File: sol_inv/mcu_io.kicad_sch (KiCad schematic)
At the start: 33 parts, among them J11 Conn_01x05, J3 Conn_01x06, J4 Conn_01x05, J5 Conn_ARM_JTAG_SWD_10, J6 Conn_01x05, J7 Conn_01x02, J8 Conn_01x08, J9 Conn_01x08, SW2 SW_Push_Dual, SW3 SW_Push_Dual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

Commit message: v0.2 components change + reference to providers
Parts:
- C21: renamed from C19; footprint Capacitor_SMD:C_1206_3216Metric -> Capacitor_SMD:C_0201_0603Metric; ComponentLink2URL (none) -> https://ro.farnell.com/wurth-elektronik/885012104002/cap-0-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
- C22: renamed from C20; footprint Capacitor_SMD:C_1206_3216Metric -> Capacitor_SMD:C_0201_0603Metric; ComponentLink2URL (none) -> https://ro.farnell.com/wurth-elektronik/885012104002/cap-0-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
- C23: renamed from C21; footprint Capacitor_SMD:C_1206_3216Metric -> Capacitor_SMD:C_0201_0603Metric; ComponentLink2URL (none) -> https://ro.farnell.com/wurth-elektronik/885012104002/cap-0-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
- C24: renamed from C22; value 18-23nF -> 22pF; ComponentLink2URL (none) -> https://ro.farnell.com/vishay/vj0805a220gxqcw1bc/cap-22pf-1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; now not fitted; now left out of the parts list
- C25: renamed from C23; value 7-11nF -> 8pF; ComponentLink2URL (none) -> https://ro.farnell.com/tdk/cga2b2np01h080d050ba/cap-8pf-50v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; now not fitted; now left out of the parts list
- C26: renamed from C24; value 18-23nF -> 22pF; ComponentLink2URL (none) -> https://ro.farnell.com/vishay/vj0805a220gxqcw1bc/cap-22pf-1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; now not fitted; now left out of the parts list
- C27: renamed from C25; value 7-11nF -> 8pF; ComponentLink2URL (none) -> https://ro.farnell.com/tdk/cga2b2np01h080d050ba/cap-8pf-50v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; now not fitted; now left out of the parts list
- D1, D2, D3: ComponentLink2URL (none) -> https://ro.farnell.com/kingbright/kp-2012syck/led-alingap-s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
- J10: renamed from J6; ComponentLink2URL (none) -> https://ro.farnell.com/multicomp-pro/2212s-05sg-85/socket-p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
- J3: footprint Connector_PinSocket_2.54mm:PinSocket_1x06_P2.54mm_Vertical -> Connector_PinHeader_2.54mm:PinHeader_1x06_P2.54mm_Vertical; ComponentLink2URL (none) -> https://ro.farnell.com/samtec/tsw-106-07-l-s/header-2-54mm-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
- J4: ComponentLink2URL (none) -> https://ro.farnell.com/multicomp-pro/2212s-05sg-85/socket-p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
- J5: ComponentLink2URL (none) -> https://ro.farnell.com/wurth-elektronik/62701021621/conn-he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
- J6: renamed from J7; ComponentLink2URL (none) -> https://ro.farnell.com/multicomp-pro/2212s-02sg-85/conn-rcp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
- J7: renamed from J8; ComponentLink2URL (none) -> https://ro.farnell.com/multicomp-pro/2212s-08sg-85/conn-rcp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
- J8: renamed from J9; ComponentLink2URL (none) -> https://ro.farnell.com/multicomp-pro/2212s-08sg-85/conn-rcp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
- J9: renamed from J11; ComponentLink2URL (none) -> https://ro.farnell.com/multicomp-pro/2212s-05sg-85/socket-p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
- R18, R19: ComponentLink2URL (none) -> https://ro.farnell.com/multicomp-pro/mcmr08x1001ftl/res-1k-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
- R20: renamed from R21; ComponentLink2URL (none) -> https://ro.farnell.com/multicomp-pro/mcmr08x1001ftl/res-1k-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
- R21: renamed from R20; ComponentLink2URL (none) -> https://ro.farnell.com/multicomp-pro/mcmr08x1001ftl/res-1k-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
- R22: ComponentLink2URL (none) -> https://ro.farnell.com/multicomp-pro/mcmr12x20r0ftl/res-20r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
- R23, R24, R25: value 82R -> 330R; footprint Resistor_SMD:R_0402_1005Metric -> Resistor_SMD:R_0603_1608Metric; ComponentLink2URL (none) -> https://ro.farnell.com/te-connectivity/crgcq0603j330r/res-3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
- R26, R27: ComponentLink2URL (none) -> https://ro.farnell.com/multicomp-pro/mcmr04x4701ftl/res-4k7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
- SW2, SW3: ComponentLink2URL (none) -> https://ro.mouser.com/ProductDetail/Omron-Electronics/B3F-1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
- U9: ComponentLink2URL (none) -> https://ro.farnell.com/infineon/psc3m5fds2acq1xqla1/mcu-32b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
- Y1: ComponentLink2URL (none) -> https://ro.farnell.com/abracon/abls-16-000mhz-d4-t/crystal-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; now not fitted; now left out of the parts list
- Y2: ComponentLink2URL (none) -> https://ro.farnell.com/iqd-frequency-products/lfxtal002997/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; now not fitted; now left out of the parts list

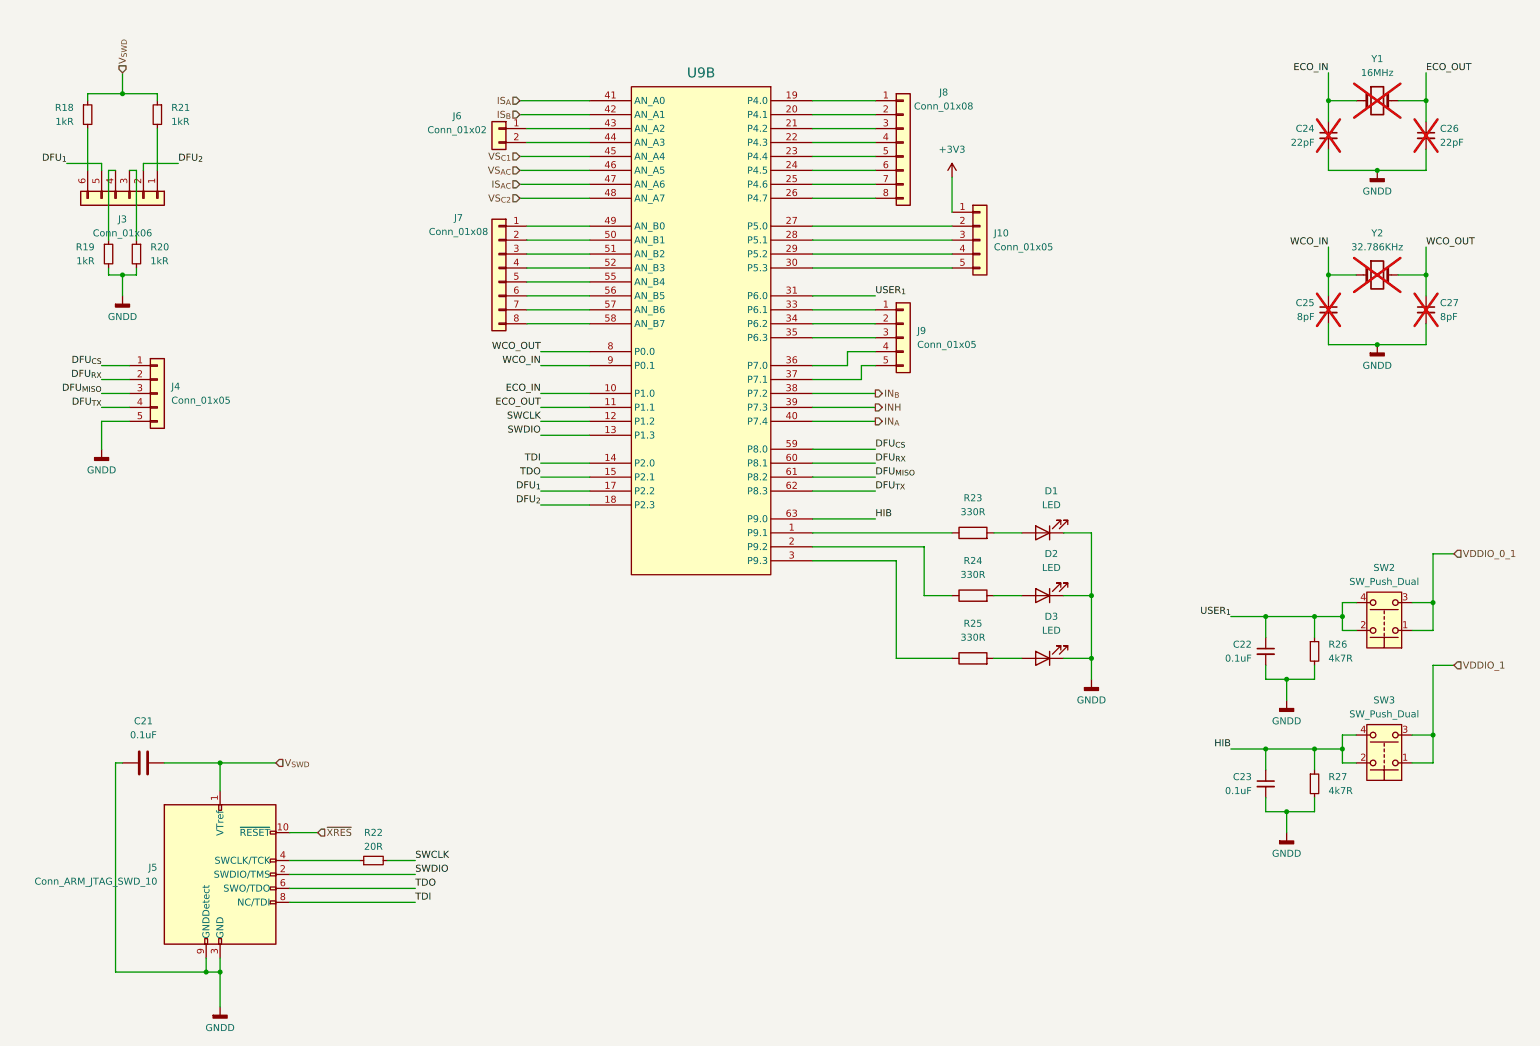
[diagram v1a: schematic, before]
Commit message: initial component placement
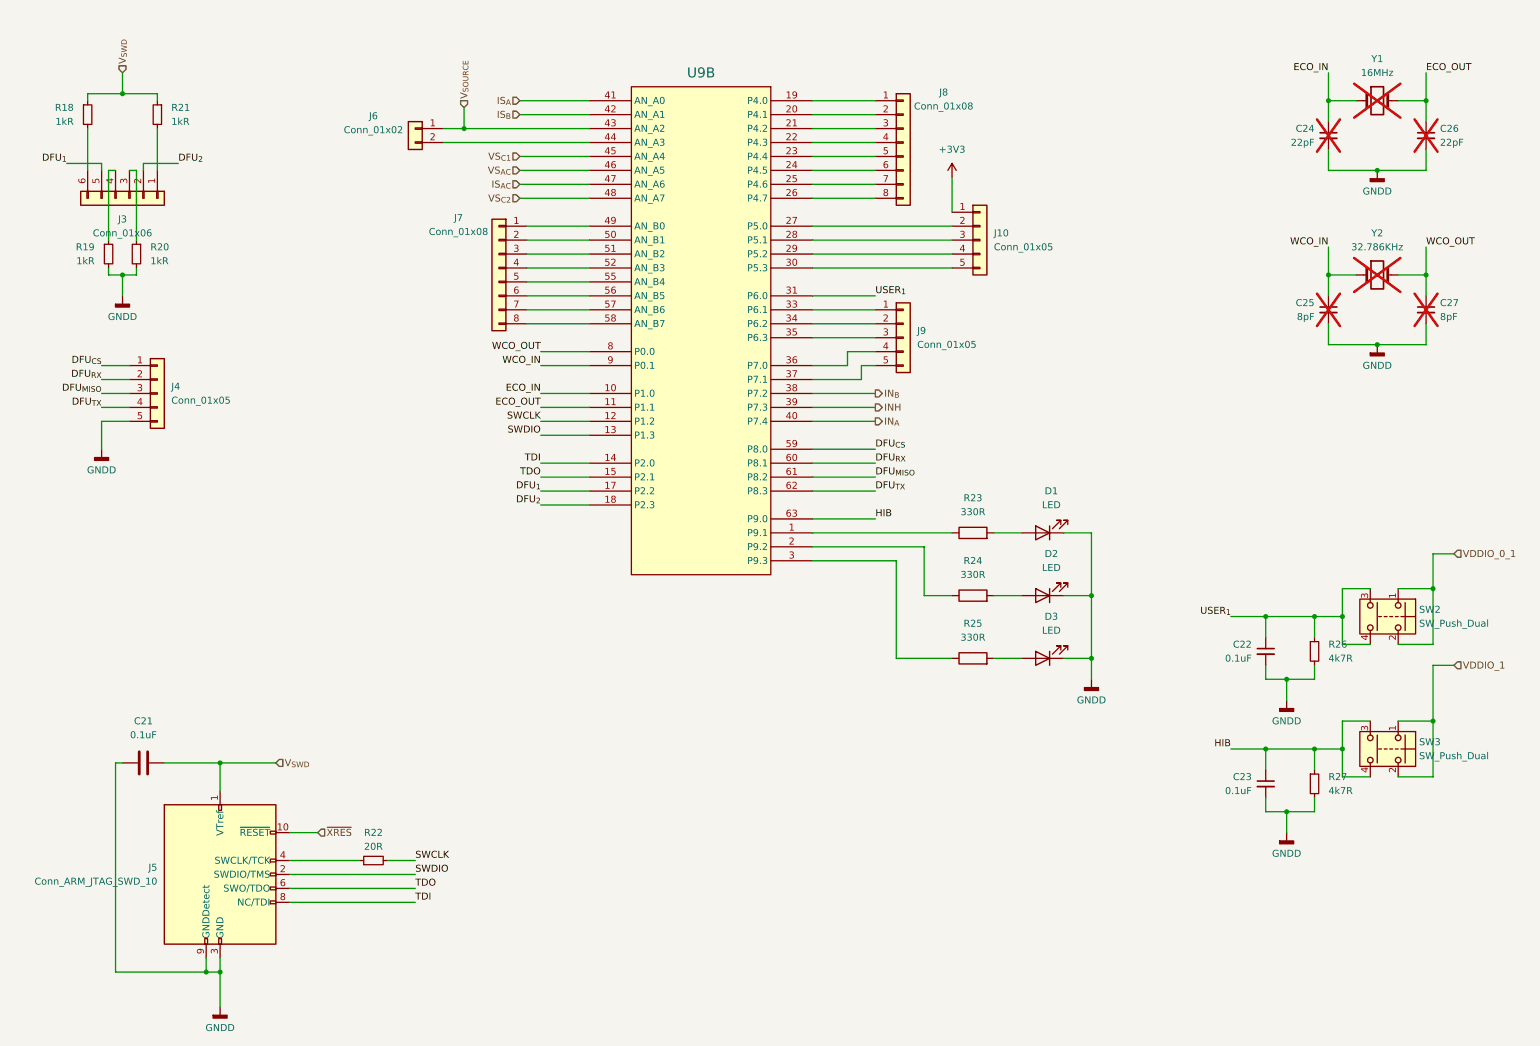
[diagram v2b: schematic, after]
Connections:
- net HIB: now also SW3.3; no longer SW3.2
- net USER_{1}: now also SW2.3; no longer SW2.2
- net VDDIO_0_1: now also SW2.2; no longer SW2.3
- net VDDIO_1: now also SW3.2; no longer SW3.3
- net V_{SOURCE}: now reaches J6.1 (Pin_1), U9.43 (AN_A2)
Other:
- moved on the sheet: J6, SW2, SW3
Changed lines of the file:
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@@
 	(title_block
 		(title "MCU I/O")
-		(date "2025-04-10")
-		(rev "0.2")
+		(date "2025-04-24")
+		(rev "0.2.1")
 		(company "Cezar-Octavian Bontaș")
 	)
@@
 	)
 	(junction
-		(at 269.24 140.97)
-		(diameter 0)
-		(color 0 0 0 0)
-	)
-	(junction
 		(at 242.57 154.94)
 		(diameter 0)
@@
 	)
 	(junction
+		(at 92.71 30.48)
+		(diameter 0)
+		(color 0 0 0 0)
+	)
+	(junction
 		(at 238.76 143.51)
 		(diameter 0)
@@
 	)
 	(junction
+		(at 269.24 114.3)
+		(diameter 0)
+		(color 0 0 0 0)
+	)
+	(junction
 		(at 242.57 130.81)
 		(diameter 0)
@@
 	)
 	(junction
-		(at 269.24 116.84)
+		(at 269.24 138.43)
 		(diameter 0)
 		(color 0 0 0 0)
@@
 	(wire
 		(pts
-			(xy 269.24 116.84) (xy 265.43 116.84)
+			(xy 262.89 114.3) (xy 269.24 114.3)
 		)
 		(stroke
@@
 	(wire
 		(pts
-			(xy 104.14 30.48) (xy 115.57 30.48)
+			(xy 88.9 30.48) (xy 92.71 30.48)
 		)
 		(stroke
@@
 	(wire
 		(pts
+			(xy 269.24 114.3) (xy 269.24 124.46)
+		)
+		(stroke
+			(width 0)
+			(type default)
+		)
+	)
+	(wire
+		(pts
 			(xy 156.21 53.34) (xy 181.61 53.34)
 		)
@@
 	(wire
 		(pts
-			(xy 252.73 146.05) (xy 252.73 143.51)
+			(xy 252.73 148.59) (xy 252.73 143.51)
 		)
 		(stroke
@@
 	(wire
 		(pts
-			(xy 252.73 119.38) (xy 252.73 116.84)
+			(xy 252.73 119.38) (xy 252.73 114.3)
 		)
 		(stroke
@@
 	(wire
 		(pts
-			(xy 26.67 83.82) (xy 26.67 88.9)
+			(xy 92.71 26.67) (xy 92.71 30.48)
 		)
 		(stroke
@@
 	(wire
 		(pts
-			(xy 167.64 43.18) (xy 156.21 43.18)
+			(xy 26.67 83.82) (xy 26.67 88.9)
 		)
 		(stroke
@@
 	(wire
 		(pts
-			(xy 265.43 121.92) (xy 269.24 121.92)
+			(xy 167.64 43.18) (xy 156.21 43.18)
 		)
 		(stroke
@@
 	(wire
 		(pts
-			(xy 269.24 107.95) (xy 269.24 116.84)
+			(xy 269.24 107.95) (xy 269.24 114.3)
 		)
 		(stroke
@@
 	(wire
 		(pts
+			(xy 262.89 148.59) (xy 269.24 148.59)
+		)
+		(stroke
+			(width 0)
+			(type default)
+		)
+	)
+	(wire
+		(pts
 			(xy 189.23 104.14) (xy 194.31 104.14)
 		)
@@
 	(wire
 		(pts
-			(xy 265.43 146.05) (xy 269.24 146.05)
+			(xy 26.67 36.83) (xy 26.67 38.1)
 		)
 		(stroke
@@
 	(wire
 		(pts
-			(xy 26.67 36.83) (xy 26.67 38.1)
+			(xy 36.83 30.48) (xy 36.83 38.1)
 		)
 		(stroke
@@
 	(wire
 		(pts
-			(xy 36.83 30.48) (xy 36.83 38.1)
+			(xy 92.71 30.48) (xy 115.57 30.48)
 		)
 		(stroke
@@
 	(wire
 		(pts
+			(xy 262.89 138.43) (xy 269.24 138.43)
+		)
+		(stroke
+			(width 0)
+			(type default)
+		)
+	)
+	(wire
+		(pts
 			(xy 162.56 73.66) (xy 162.56 71.12)
 		)
@@
 	(wire
 		(pts
+			(xy 252.73 138.43) (xy 252.73 143.51)
+		)
+		(stroke
+			(width 0)
+			(type default)
+		)
+	)
+	(wire
+		(pts
 			(xy 176.53 115.57) (xy 181.61 115.57)
 		)
@@
 	(wire
 		(pts
-			(xy 252.73 121.92) (xy 252.73 119.38)
+			(xy 252.73 124.46) (xy 252.73 119.38)
 		)
 		(stroke
@@
 	(wire
 		(pts
-			(xy 104.14 33.02) (xy 115.57 33.02)
+			(xy 88.9 33.02) (xy 115.57 33.02)
 		)
 		(stroke
@@
 	(wire
 		(pts
-			(xy 255.27 121.92) (xy 252.73 121.92)
+			(xy 252.73 124.46) (xy 257.81 124.46)
 		)
 		(stroke
@@
 	(wire
 		(pts
-			(xy 269.24 116.84) (xy 269.24 121.92)
-		)
-		(stroke
-			(width 0)
-			(type default)
-		)
-	)
-	(wire
-		(pts
 			(xy 156.21 91.44) (xy 167.64 91.44)
 		)
@@
 	(wire
 		(pts
-			(xy 252.73 140.97) (xy 255.27 140.97)
+			(xy 252.73 138.43) (xy 257.81 138.43)
 		)
 		(stroke
@@
 	(wire
 		(pts
-			(xy 252.73 116.84) (xy 255.27 116.84)
+			(xy 252.73 114.3) (xy 257.81 114.3)
 		)
 		(stroke
@@
 	(wire
 		(pts
-			(xy 269.24 140.97) (xy 265.43 140.97)
+			(xy 26.67 81.28) (xy 31.75 81.28)
 		)
 		(stroke
@@
 	(wire
 		(pts
-			(xy 26.67 81.28) (xy 31.75 81.28)
+			(xy 30.48 20.32) (xy 30.48 24.13)
 		)
 		(stroke
@@
 	(wire
 		(pts
-			(xy 30.48 20.32) (xy 30.48 24.13)
+			(xy 262.89 124.46) (xy 269.24 124.46)
 		)
 		(stroke
@@
 	(wire
 		(pts
+			(xy 269.24 138.43) (xy 269.24 148.59)
+		)
+		(stroke
+			(width 0)
+			(type default)
+		)
+	)
+	(wire
+		(pts
 			(xy 24.13 30.48) (xy 24.13 38.1)
 		)
@@
 	(wire
 		(pts
-			(xy 255.27 146.05) (xy 252.73 146.05)
+			(xy 252.73 148.59) (xy 257.81 148.59)
 		)
 		(stroke
@@
 	(wire
 		(pts
-			(xy 252.73 143.51) (xy 252.73 140.97)
-		)
-		(stroke
-			(width 0)
-			(type default)
-		)
-	)
-	(wire
-		(pts
 			(xy 30.48 57.15) (xy 33.02 57.15)
 		)
@@
 	(wire
 		(pts
-			(xy 269.24 128.27) (xy 269.24 140.97)
-		)
-		(stroke
-			(width 0)
-			(type default)
-		)
-	)
-	(wire
-		(pts
 			(xy 238.76 119.38) (xy 247.65 119.38)
 		)
@@
 	(wire
 		(pts
-			(xy 269.24 140.97) (xy 269.24 146.05)
+			(xy 269.24 128.27) (xy 269.24 138.43)
 		)
 		(stroke
@@
 		)
 	)
+	(hierarchical_label "V_{SOURCE}"
+		(shape input)
+		(at 92.71 26.67 90)
+		(effects
+			(font
+				(size 1.27 1.27)
+			)
+			(justify left)
+		)
+	)
 	(hierarchical_label "VS_{C2}"
 		(shape input)
@@
 	(symbol
 		(lib_id "Switch:SW_Push_Dual")
-		(at 260.35 143.51 180)
+		(at 260.35 143.51 270)
 		(unit 1)
 		(exclude_from_sim no)
@@
 		(fields_autoplaced yes)
 		(property "Reference" "SW3"
-			(at 260.35 134.62 0)
+			(at 266.7 142.2399 90)
 			(effects
 				(font
 					(size 1.27 1.27)
 				)
+				(justify left)
 			)
 		)
 		(property "Value" "SW_Push_Dual"
-			(at 260.35 137.16 0)
+			(at 266.7 144.7799 90)
 			(effects
 				(font
 					(size 1.27 1.27)
 				)
+				(justify left)
 			)
 		)
 		(property "Footprint" "B3F-1000:SW_B3F-1000_OMR"
-			(at 260.35 151.13 0)
+			(at 267.97 143.51 0)
 			(effects
 				(font
@@
 	(symbol
 		(lib_id "Connector_Generic:Conn_01x02")
-		(at 99.06 30.48 0)
+		(at 83.82 30.48 0)
 		(mirror y)
 		(unit 1)
@@
 		(dnp no)
 		(property "Reference" "J6"
-			(at 91.44 28.194 0)
+			(at 76.2 28.194 0)
 			(effects
 				(font
@@
 		)
 		(property "Value" "Conn_01x02"
-			(at 91.44 30.734 0)
+			(at 76.2 30.734 0)
 			(effects
 				(font
@@
 		)
 		(property "Footprint" "Connector_PinSocket_2.54mm:PinSocket_1x02_P2.54mm_Vertical"
-			(at 99.06 30.48 0)
+			(at 83.82 30.48 0)
 			(effects
 				(font
@@
 		)
 		(property "Datasheet" "https://4donline.ihs.com/images/VipMasterIC/IC/SCMP/SCMP-S-A0019040871/SCMP-S-A0019041026-1.pdf?hkey=6D3A4C79FDBF58556ACFDE234799DDF0"
-			(at 99.06 30.48 0)
+			(at 83.82 30.48 0)
 			(effects
 				(font
@@
 		)
 		(property "Description" "Generic connector, single row, 01x02, script generated (kicad-library-utils/schlib/autogen/connector/)"
-			(at 99.06 30.48 0)
+			(at 83.82 30.48 0)
 			(effects
 				(font
@@
 		)
 		(property "ComponentLink1URL" ""
-			(at 99.06 30.48 0)
+			(at 83.82 30.48 0)
 			(effects
 				(font
@@
 		)
 		(property "ComponentLink2URL" "https://ro.farnell.com/multicomp-pro/2212s-02sg-85/conn-rcpt-2pos-1row-2-54mm/dp/1593458"
-			(at 99.06 30.48 0)
+			(at 83.82 30.48 0)
 			(effects
 				(font
@@
 	(symbol
 		(lib_id "Switch:SW_Push_Dual")
-		(at 260.35 119.38 180)
+		(at 260.35 119.38 270)
 		(unit 1)
 		(exclude_from_sim no)
@@
 		(fields_autoplaced yes)
 		(property "Reference" "SW2"
-			(at 260.35 110.49 0)
+			(at 266.7 118.1099 90)
 			(effects
 				(font
 					(size 1.27 1.27)
 				)
+				(justify left)
 			)
 		)
 		(property "Value" "SW_Push_Dual"
-			(at 260.35 113.03 0)
+			(at 266.7 120.6499 90)
 			(effects
 				(font
 					(size 1.27 1.27)
 				)
+				(justify left)
 			)
 		)
 		(property "Footprint" "B3F-1000:SW_B3F-1000_OMR"
-			(at 260.35 127 0)
+			(at 267.97 119.38 0)
 			(effects
 				(font
